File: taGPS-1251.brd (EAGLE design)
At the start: 41.4 x 80 mm, 84 parts, among them IC1 MSP430FR698X(1)80-PIN_PN, IC3 FT232RL

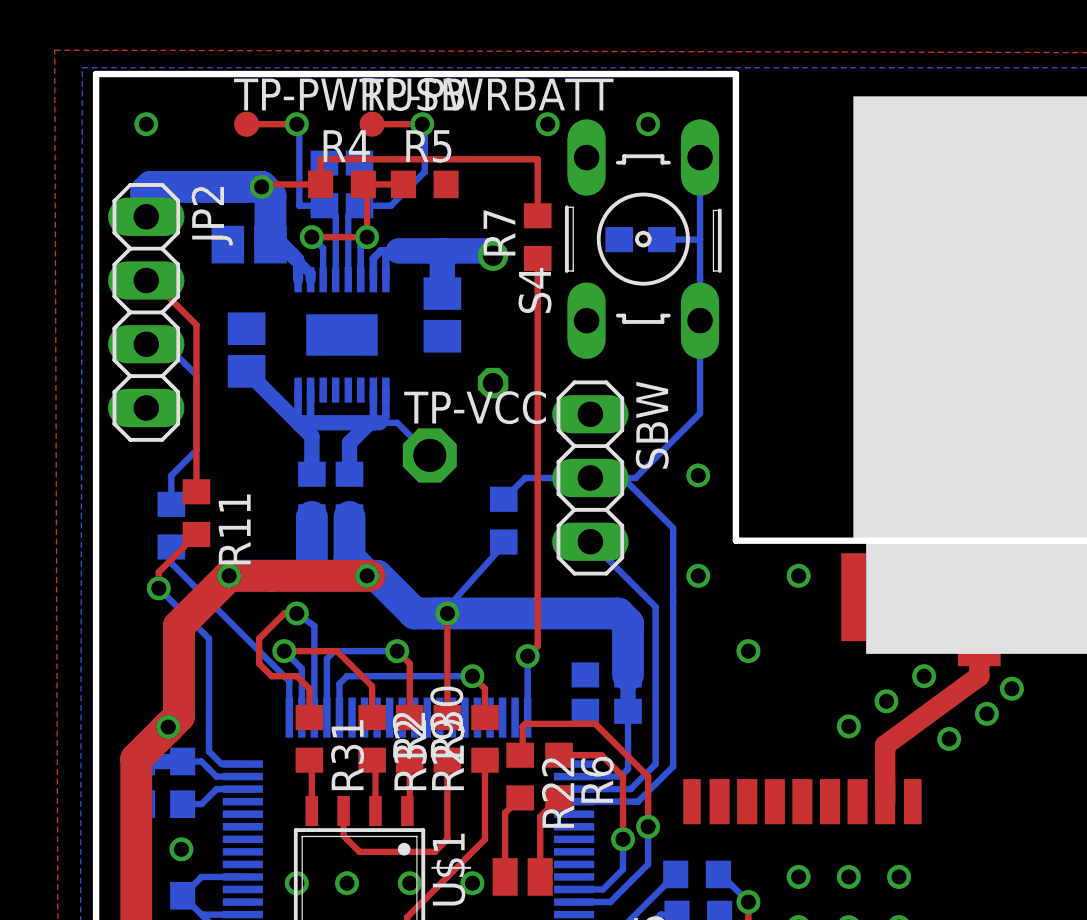
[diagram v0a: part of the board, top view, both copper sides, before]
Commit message: Fix MCU RX/TX pinheader position, polish boards
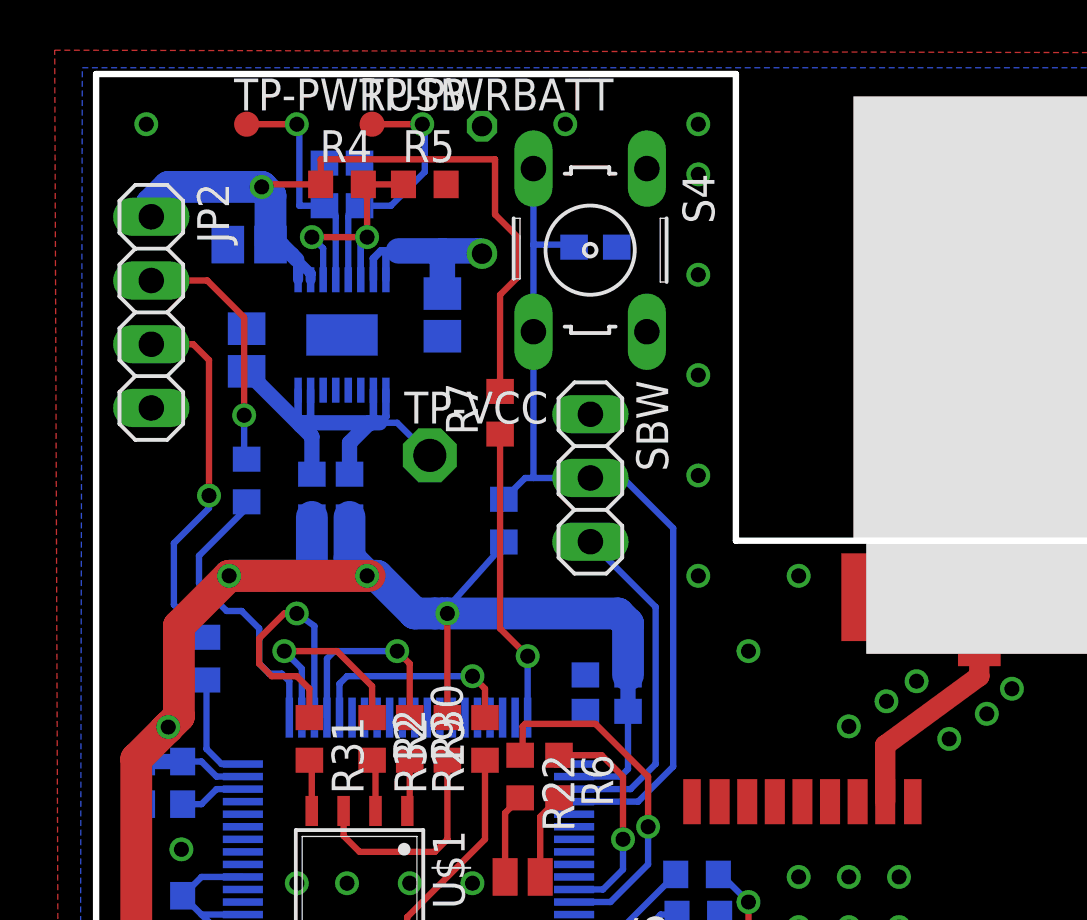
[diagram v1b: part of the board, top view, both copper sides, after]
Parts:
- moved R7 7.16 mm to (16.1, 66.5)
- moved R11 5.81 mm to (4.40, 56.7), flipped to the bottom
- moved G2 5.18 mm to (15.4, 75.4), turned to 90 degrees
- moved R19 3.50 mm to (6.00, 63.8)
- moved S4 2.17 mm to (19.7, 73.0), turned to 270 degrees
- moved C15 1.82 mm to (19.9, 73.1), turned to 180 degrees
- moved JP2 0.20 mm to (2.20, 70.5)
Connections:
- net MCU-TX-FT232: now also JP2.3; no longer JP2.2
- net N$8: now also JP2.2; no longer JP2.3
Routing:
- net N$2: track 11.7 -> 4.45 mm, vias 1 -> 0
- net PWR-USB-SENSE: track 19.3 -> 12.4 mm
- net VCCUSBGPS: track 25.8 -> 31.3 mm
- net MCU-TX-FT232: track 9.38 -> 14.7 mm, vias 0 -> 1
- net SBW-TDO/TDI: track 39.5 -> 36.0 mm
- net MCU-RX-FT232: track 8.75 -> 11.5 mm
- net N$8: track 8.07 -> 10.0 mm, vias 0 -> 1
- net GND: vias 39 -> 42
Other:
- board text added: "GND TX RX VCC"

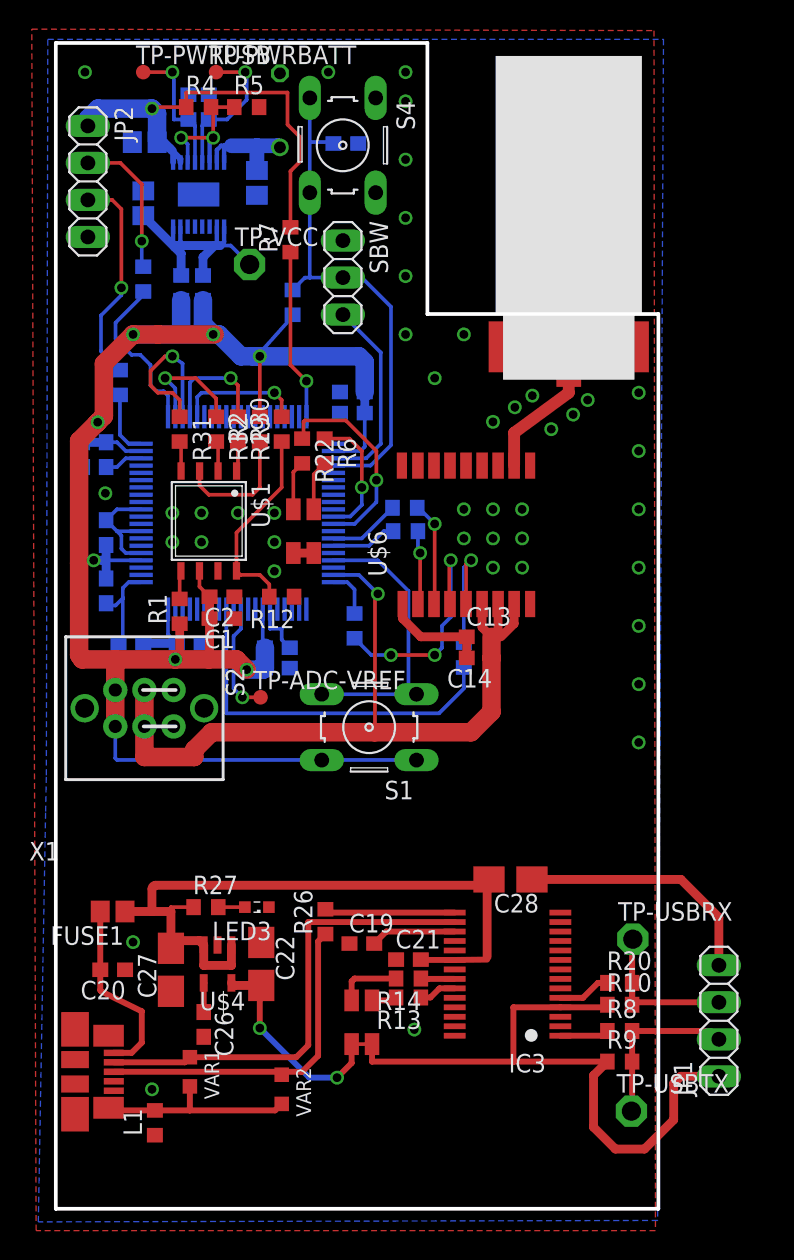
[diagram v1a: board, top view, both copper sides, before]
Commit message: Replace FUSE package to 1812
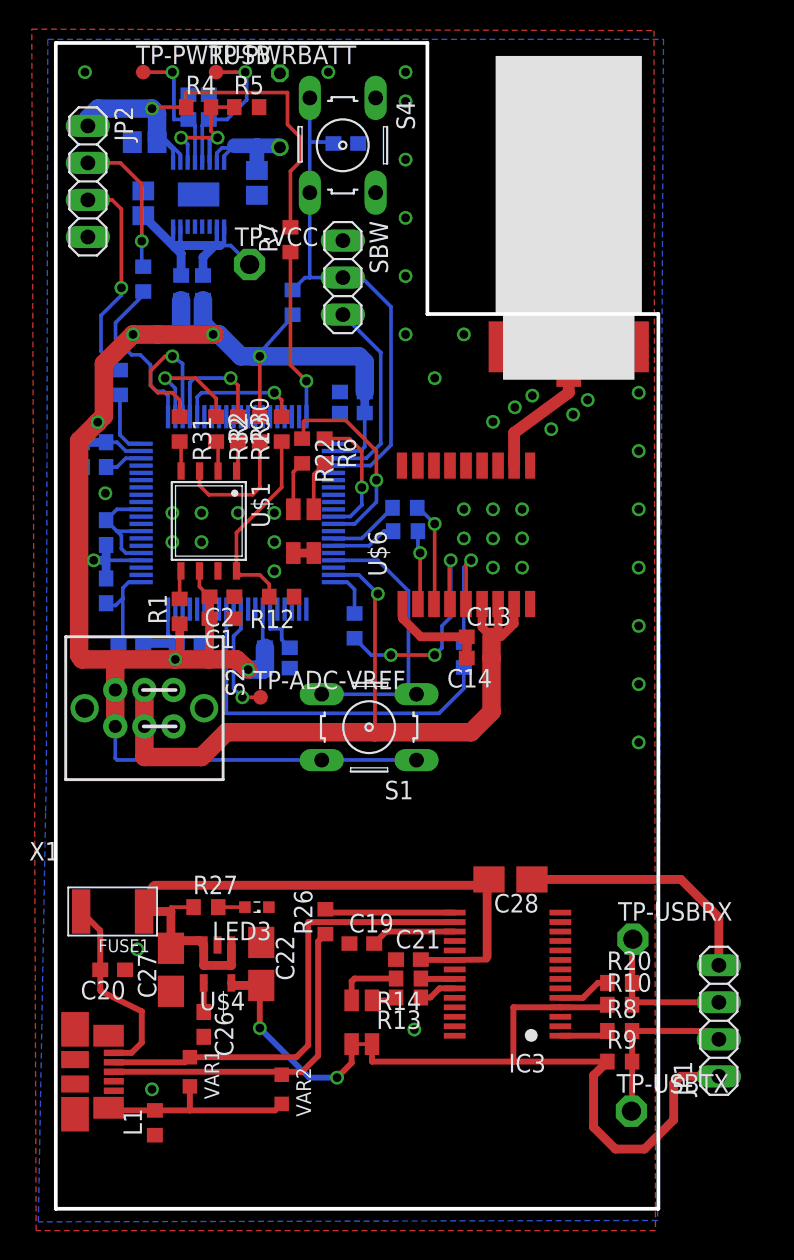
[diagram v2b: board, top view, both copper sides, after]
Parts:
- FUSE1: value 500mA -> SMD1206R500SF; device tagps:R0805 -> tagps:F1812
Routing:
- net VCCUSBGPS: track 31.3 -> 32.8 mm
- net VBUS: track 49.3 -> 48.0 mm
- net N$7: track 11.5 -> 12.2 mm
- net N$22: track 13.0 -> 13.5 mm

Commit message: Check rules acc seeed studio
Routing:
- net GND: vias 42 -> 44
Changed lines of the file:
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@@
 <setting verticaltext="up"/>
 </settings>
-<grid distance="0.1" unitdist="mm" unit="mm" style="lines" multiple="1" display="yes" altdistance="0.025" altunitdist="inch" altunit="inch"/>
+<grid distance="10" unitdist="mil" unit="mil" style="lines" multiple="1" display="yes" altdistance="0.025" altunitdist="inch" altunit="inch"/>
 <layers>
 <layer number="1" name="Top" color="4" fill="1" visible="yes" active="yes"/>
@@
 <classes>
 <class number="0" name="signal" width="0.254" drill="0.254">
-<clearance class="0" value="0.15"/>
+<clearance class="0" value="0.0254"/>
 </class>
-<class number="1" name="charimp50" width="0.254" drill="0.254">
-<clearance class="1" value="0.15"/>
+<class number="1" name="charimp50" width="0.6096" drill="0.254">
+<clearance class="1" value="0.5588"/>
 </class>
 <class number="2" name="conect" width="0.254" drill="0.254">
 </class>
 </classes>
-<designrules name="LaenPCBOrder *">
+<designrules name="SeeedStudio_2layer_DRU_no_angle_20140221">
 <description language="de">&lt;b&gt;EAGLE Design Rules&lt;/b&gt;
 &lt;p&gt;
@@
 Einstellungen hier und speichern die Design Rules unter
 einem neuen Namen ab.</description>
-<description language="en">&lt;b&gt;Laen's PCB Order Design Rules&lt;/b&gt;
+<description language="en">&lt;b&gt;EAGLE Design Rules&lt;/b&gt;
 &lt;p&gt;
-Please make sure your boards conform to these design rules.</description>
+The default Design Rules have been set to cover
+a wide range of applications. Your particular design
+may have different requirements, so please make the
+necessary adjustments and save your customized
+design rules under a new name.</description>
+<description language="zh">&lt;b&gt;Seeed Studio EAGLE Design Rules&lt;/b&gt;
+</description>
 <param name="layerSetup" value="(1*16)"/>
-<param name="mtCopper" value="0.0356mm 0.0356mm 0.0356mm 0.0356mm 0.0356mm 0.0356mm 0.0356mm 0.0356mm 0.0356mm 0.0356mm 0.0356mm 0.0356mm 0.0356mm 0.0356mm 0.0356mm 0.0356mm"/>
-<param name="mtIsolate" value="1.5011mm 0.1499mm 0.2007mm 0.1499mm 0.2007mm 0.1499mm 0.2007mm 0.1499mm 0.2007mm 0.1499mm 0.2007mm 0.1499mm 0.2007mm 0.1499mm 0.2007mm"/>
-<param name="mdWireWire" value="1mil"/>
-<param name="mdWirePad" value="1mil"/>
-<param name="mdWireVia" value="1mil"/>
-<param name="mdPadPad" value="1mil"/>
-<param name="mdPadVia" value="1mil"/>
-<param name="mdViaVia" value="1mil"/>
-<param name="mdSmdPad" value="1mil"/>
-<param name="mdSmdVia" value="1mil"/>
-<param name="mdSmdSmd" value="1mil"/>
+<param name="mtCopper" value="0.035mm 0.0175mm 0.035mm 0.035mm 0.035mm 0.035mm 0.035mm 0.035mm 0.035mm 0.035mm 0.035mm 0.035mm 0.035mm 0.035mm 0.0175mm 0.035mm"/>
+<param name="mtIsolate" value="1.5mm 1.1mm 0.2mm 0.15mm 0.2mm 0.15mm 0.2mm 0.15mm 0.2mm 0.15mm 0.2mm 0.15mm 0.2mm 0.15mm 0.2mm"/>
+<param name="mdWireWire" value="6mil"/>
+<param name="mdWirePad" value="6mil"/>
+<param name="mdWireVia" value="6mil"/>
+<param name="mdPadPad" value="6mil"/>
+<param name="mdPadVia" value="6mil"/>
+<param name="mdViaVia" value="6mil"/>
+<param name="mdSmdPad" value="0mil"/>
+<param name="mdSmdVia" value="0mil"/>
+<param name="mdSmdSmd" value="0mil"/>
 <param name="mdViaViaSameLayer" value="8mil"/>
 <param name="mnLayersViaInSmd" value="2"/>
-<param name="mdCopperDimension" value="6mil"/>
-<param name="mdDrill" value="6mil"/>
+<param name="mdCopperDimension" value="10mil"/>
+<param name="mdDrill" value="10mil"/>
 <param name="mdSmdStop" value="0mil"/>
 <param name="msWidth" value="6mil"/>
-<param name="msDrill" value="13mil"/>
-<param name="msMicroVia" value="13mil"/>
+<param name="msDrill" value="12mil"/>
+<param name="msMicroVia" value="12mil"/>
 <param name="msBlindViaRatio" value="0.5"/>
 <param name="rvPadTop" value="0.25"/>
@@
 <param name="rvMicroViaOuter" value="0.25"/>
 <param name="rvMicroViaInner" value="0.25"/>
-<param name="rlMinPadTop" value="7mil"/>
+<param name="rlMinPadTop" value="10mil"/>
 <param name="rlMaxPadTop" value="20mil"/>
-<param name="rlMinPadInner" value="7mil"/>
+<param name="rlMinPadInner" value="10mil"/>
 <param name="rlMaxPadInner" value="20mil"/>
-<param name="rlMinPadBottom" value="7mil"/>
+<param name="rlMinPadBottom" value="10mil"/>
 <param name="rlMaxPadBottom" value="20mil"/>
-<param name="rlMinViaOuter" value="7mil"/>
+<param name="rlMinViaOuter" value="6mil"/>
 <param name="rlMaxViaOuter" value="20mil"/>
-<param name="rlMinViaInner" value="7mil"/>
+<param name="rlMinViaInner" value="6mil"/>
 <param name="rlMaxViaInner" value="20mil"/>
 <param name="rlMinMicroViaOuter" value="4mil"/>
@@
 <param name="psTop" value="-1"/>
 <param name="psBottom" value="-1"/>
-<param name="psFirst" value="-1"/>
+<param name="psFirst" value="0"/>
 <param name="psElongationLong" value="100"/>
 <param name="psElongationOffset" value="100"/>
-<param name="mvStopFrame" value="0"/>
+<param name="mvStopFrame" value="1"/>
 <param name="mvCreamFrame" value="0"/>
-<param name="mlMinStopFrame" value="0mil"/>
-<param name="mlMaxStopFrame" value="0mil"/>
+<param name="mlMinStopFrame" value="2mil"/>
+<param name="mlMaxStopFrame" value="2mil"/>
 <param name="mlMinCreamFrame" value="0mil"/>
 <param name="mlMaxCreamFrame" value="0mil"/>
-<param name="mlViaStopLimit" value="0mil"/>
+<param name="mlViaStopLimit" value="100mil"/>
 <param name="srRoundness" value="0"/>
 <param name="srMinRoundness" value="0mil"/>
@@
 <param name="checkAngle" value="0"/>
 <param name="checkFont" value="1"/>
-<param name="checkRestrict" value="1"/>
+<param name="checkRestrict" value="0"/>
 <param name="useDiameter" value="13"/>
 <param name="maxErrors" value="50"/>
@@
 <wire x1="23.8" y1="40.5" x2="23.8" y2="41.5" width="0.6096" layer="1"/>
 <wire x1="28.2" y1="37.8" x2="28.2" y2="39.25" width="0.6096" layer="1"/>
-<via x="32.7" y="55.8" extent="1-16" drill="0.6"/>
+<via x="32.004" y="55.88" extent="1-16" drill="0.6"/>
 <via x="24" y="78" extent="1-16" drill="0.6"/>
 <via x="18.7" y="78" extent="1-16" drill="0.6"/>
@@
 <wire x1="45.5" y1="20" x2="42.9" y2="22.6" width="0.6096" layer="1"/>
 <wire x1="42.9" y1="22.6" x2="32.675" y2="22.6" width="0.6096" layer="1"/>
-<via x="31.5" y="55" extent="1-16" drill="0.6"/>
-<via x="30" y="54" extent="1-16" drill="0.6"/>
-<via x="36.5" y="55.5" extent="1-16" drill="0.6"/>
-<via x="35.5" y="54.5" extent="1-16" drill="0.6"/>
-<via x="34" y="53.5" extent="1-16" drill="0.6"/>
+<via x="30.988" y="55.118" extent="1-16" drill="0.6"/>
+<via x="29.972" y="54.356" extent="1-16" drill="0.6"/>
+<via x="37.084" y="55.626" extent="1-16" drill="0.6"/>
+<via x="36.322" y="54.864" extent="1-16" drill="0.6"/>
+<via x="35.306" y="54.102" extent="1-16" drill="0.6"/>
 <via x="40" y="40" extent="1-16" drill="0.6"/>
 <via x="40" y="44" extent="1-16" drill="0.6"/>
@@
 <via x="24" y="72" extent="1-16" drill="0.6"/>
 <via x="24" y="76" extent="1-16" drill="0.6"/>
+<via x="34.29" y="53.34" extent="1-16" drill="0.6"/>
+<via x="29.972" y="53.086" extent="1-16" drill="0.6"/>
 </signal>
 <signal name="SBW-TDO/TDI">
@@
 <contactref element="U$6" pad="11"/>
 <contactref element="U$5" pad="P$2"/>
-<wire x1="31.45" y1="51" x2="31.45" y2="53.25" width="0.8128" layer="1"/>
-<wire x1="31.45" y1="53.25" x2="35.2" y2="56" width="0.8128" layer="1"/>
-<wire x1="35.2" y1="56" x2="35.2" y2="58.15" width="0.8128" layer="1"/>
+<wire x1="31.45" y1="51" x2="31.45" y2="53.25" width="0.6096" layer="1"/>
+<wire x1="31.45" y1="53.25" x2="35.2" y2="56" width="0.6096" layer="1"/>
+<wire x1="35.2" y1="56" x2="35.2" y2="58.15" width="0.6096" layer="1"/>
 </signal>
 <signal name="N$48">
